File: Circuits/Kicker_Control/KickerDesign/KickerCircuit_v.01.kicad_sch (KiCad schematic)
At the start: 8 parts, among them J1 Solenoid, Q1 NMOS, U1 NSL-32

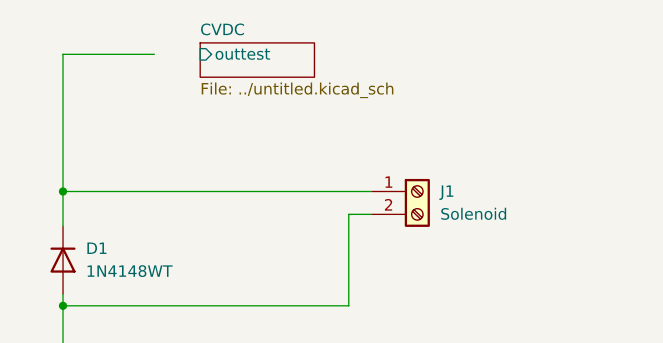
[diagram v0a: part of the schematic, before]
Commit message: Changed the Kicker subcircuit link
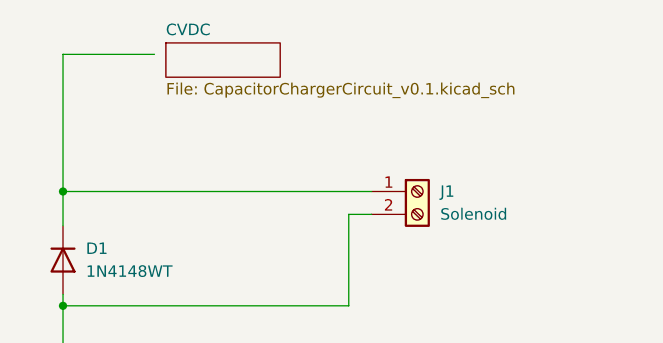
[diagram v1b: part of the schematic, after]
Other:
- sheet CVDC: file ../untitled.kicad_sch -> CapacitorChargerCircuit_v0.1.kicad_sch
- sheet CVDC ports: added none; removed outtest
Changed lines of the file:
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@@
 	)
 	(sheet
-		(at 165.1 60.96)
+		(at 161.29 60.96)
 		(size 12.7 3.81)
 		(fields_autoplaced yes)
@@
 		)
 		(property "Sheetname" "CVDC"
-			(at 165.1 60.2484 0)
+			(at 161.29 60.2484 0)
 			(effects
 				(font
@@
 			)
 		)
-		(property "Sheetfile" "../untitled.kicad_sch"
-			(at 165.1 65.3546 0)
+		(property "Sheetfile" "CapacitorChargerCircuit_v0.1.kicad_sch"
+			(at 161.29 65.3546 0)
 			(effects
 				(font
@@
 			)
 		)
-		(pin "outtest" input
-			(at 165.1 62.23 180)
-			(effects
-				(font
-					(size 1.27 1.27)
-				)
-				(justify left)
-			)
-		)
 		(instances
-			(project "KickerCircuit_v01"
+			(project "KickerCircuit_v.01"
 				(path "/a7a112f4-0a48-49be-a5c8-a832ec6f12fb"
 					(page "2")

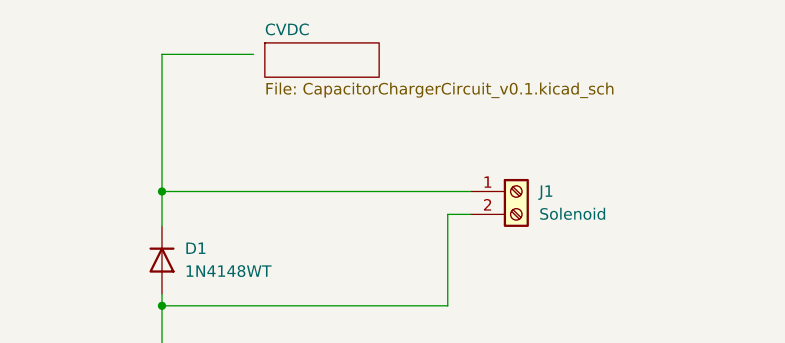
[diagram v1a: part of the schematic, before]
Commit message: Added input to the Kicker circuit
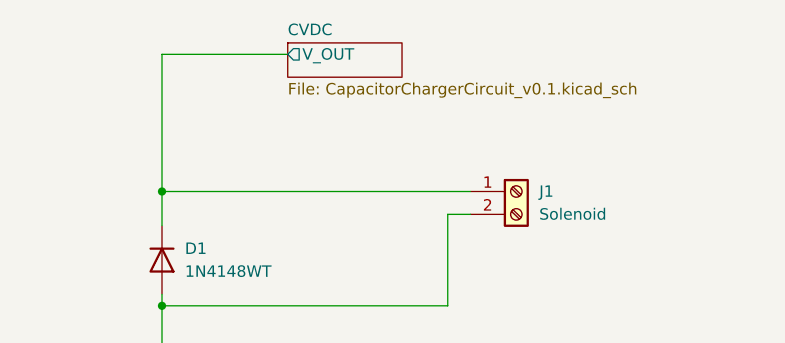
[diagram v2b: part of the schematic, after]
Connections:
- net CVDC/V_OUT: now reaches D1.1 (K), J1.1 (Pin_1)
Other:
- sheet CVDC ports: added V_OUT; removed none
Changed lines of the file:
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@@
 	(wire
 		(pts
-			(xy 160.02 62.23) (xy 149.86 62.23)
+			(xy 149.86 62.23) (xy 163.83 62.23)
 		)
 		(stroke
@@
 	)
 	(sheet
-		(at 161.29 60.96)
+		(at 163.83 60.96)
 		(size 12.7 3.81)
 		(fields_autoplaced yes)
@@
 		)
 		(property "Sheetname" "CVDC"
-			(at 161.29 60.2484 0)
+			(at 163.83 60.2484 0)
 			(effects
 				(font
@@
 		)
 		(property "Sheetfile" "CapacitorChargerCircuit_v0.1.kicad_sch"
-			(at 161.29 65.3546 0)
+			(at 163.83 65.3546 0)
 			(effects
 				(font
@@
 			)
 		)
+		(pin "V_OUT" output
+			(at 163.83 62.23 180)
+			(effects
+				(font
+					(size 1.27 1.27)
+				)
+				(justify left)
+			)
+		)

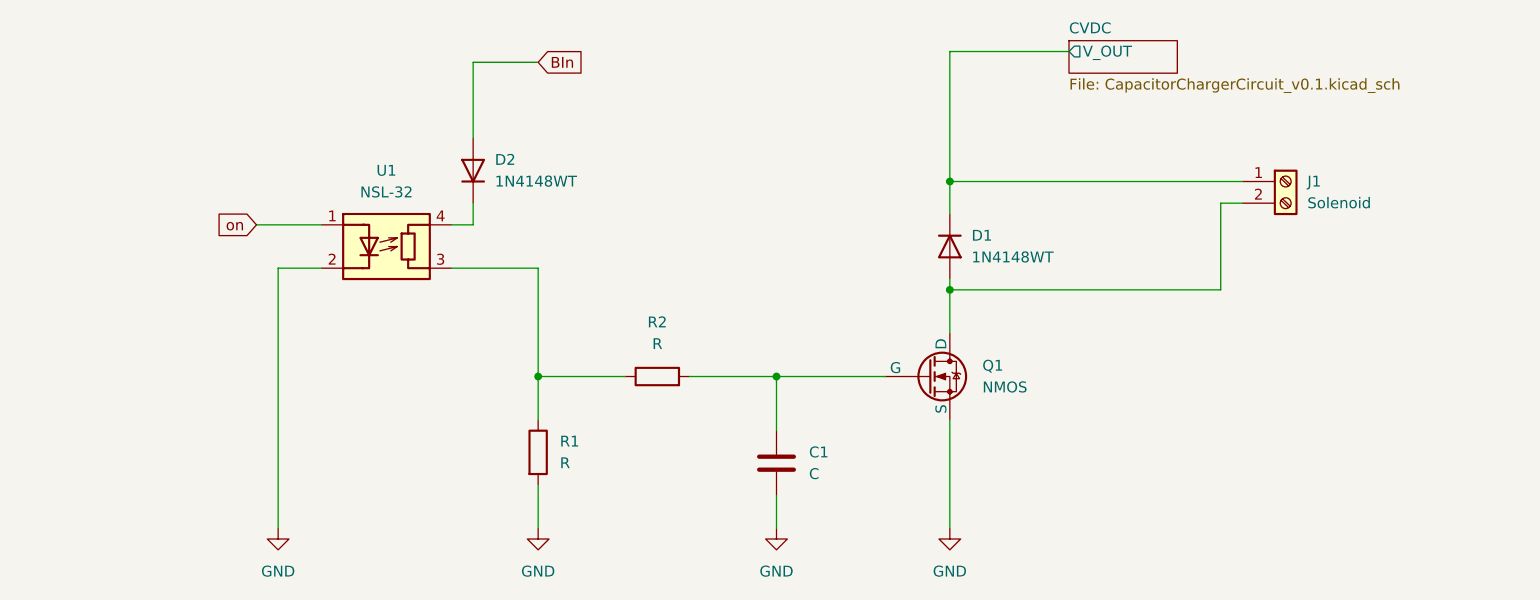
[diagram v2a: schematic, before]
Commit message: Updated kicker circuit
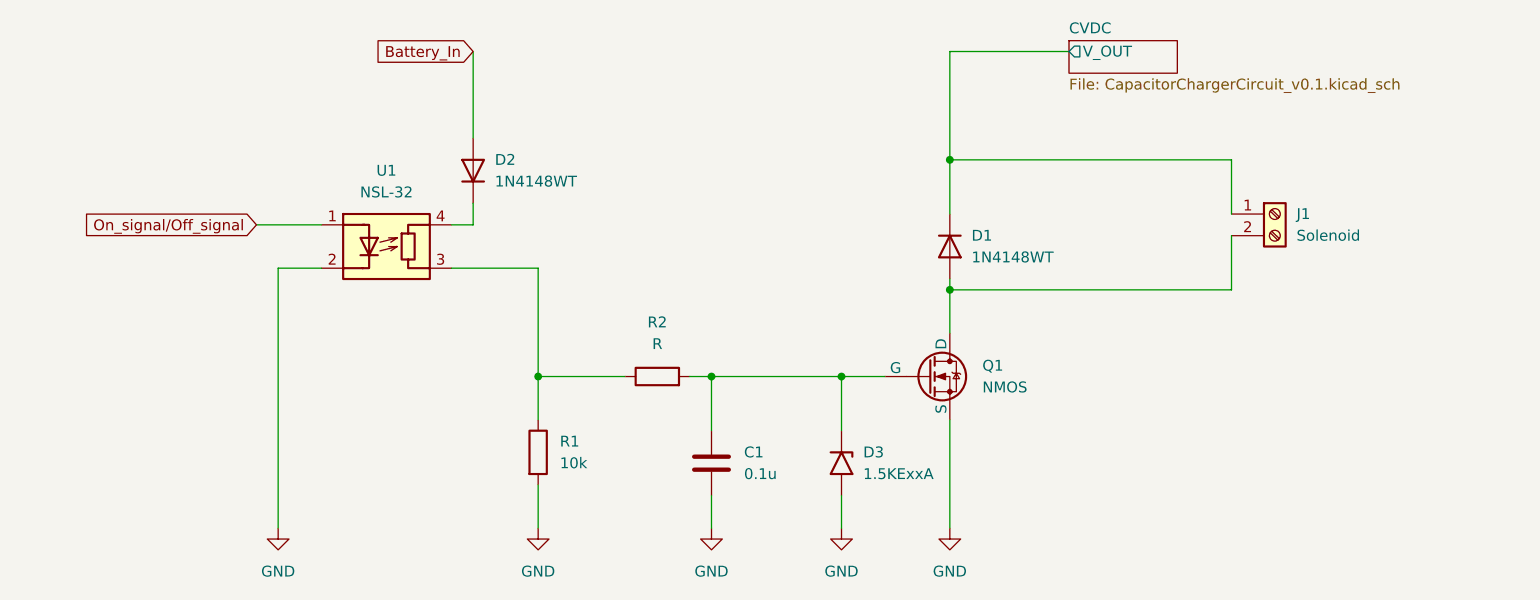
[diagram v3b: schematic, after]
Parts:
- added D3: 1.5KExxA, Diode_THT:D_DO-201AE_P15.24mm_Horizontal, symbol Diode:1.5KExxA
- C1: value C -> 0.1u
- R1: value R -> 10k
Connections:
- net GND: now also D3.2 (A2)
- net at C1.1, Q1.2 (G), R2.2: now also D3.1 (A1)
- net BIn renamed Battery_In
- net on renamed On_signal/Off_signal
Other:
- moved on the sheet: C1, J1
